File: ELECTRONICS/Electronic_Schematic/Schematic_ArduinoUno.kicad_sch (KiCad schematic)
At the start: 25 parts

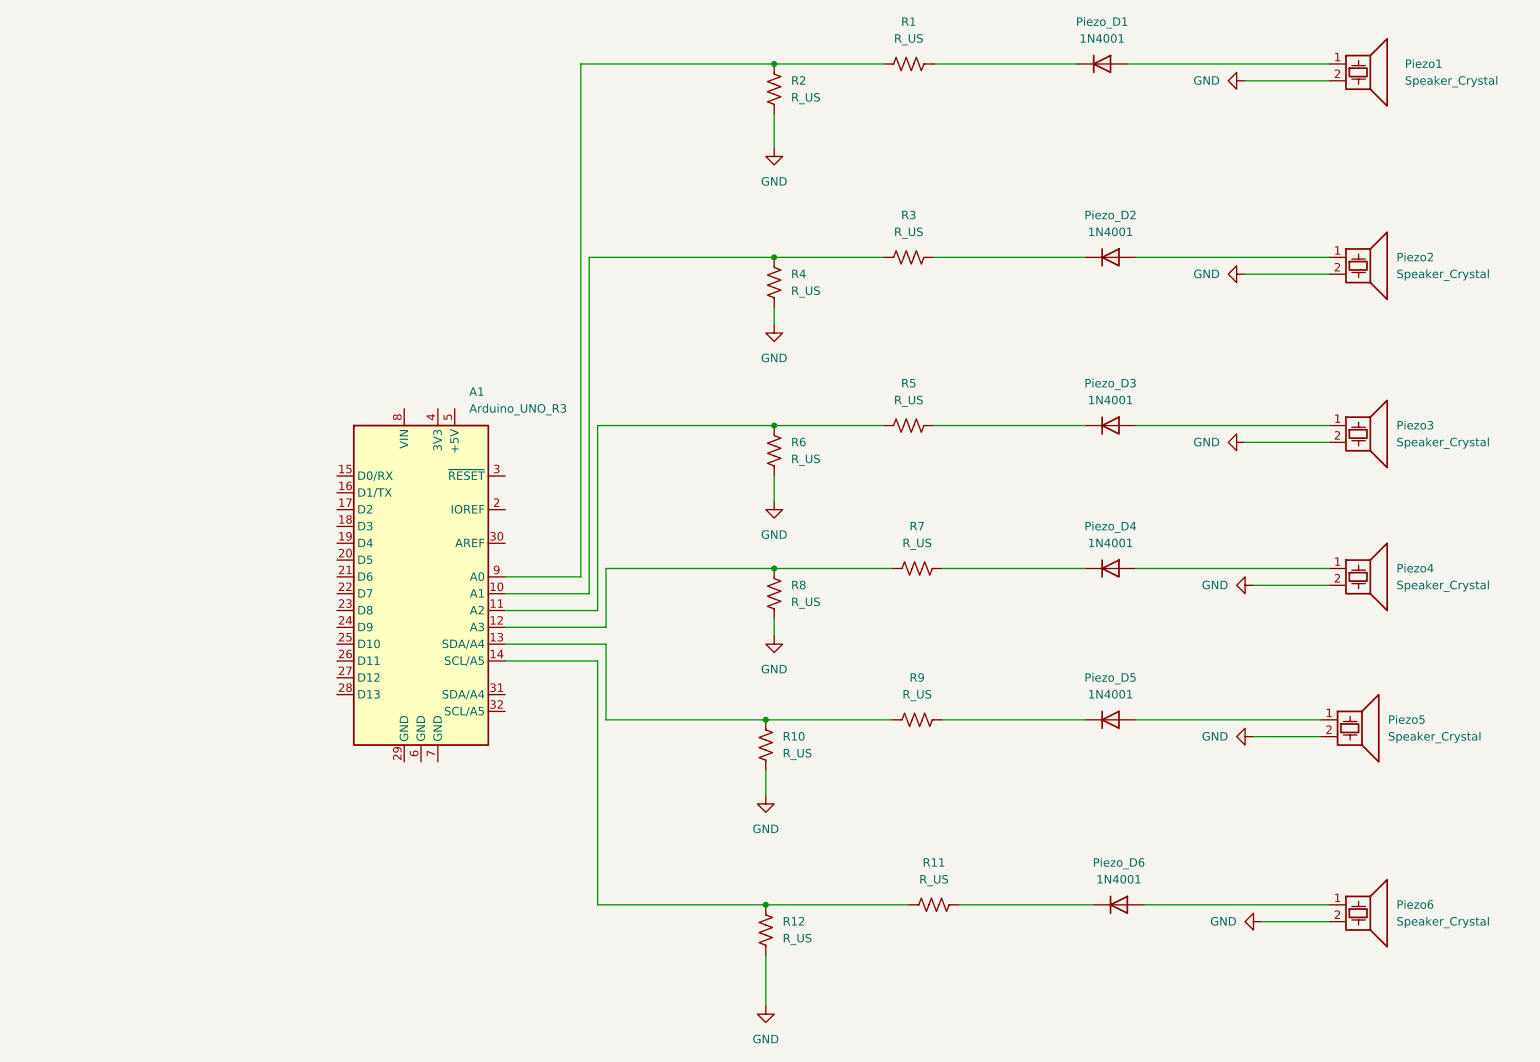
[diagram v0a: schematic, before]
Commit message: added revision 3 of schematic
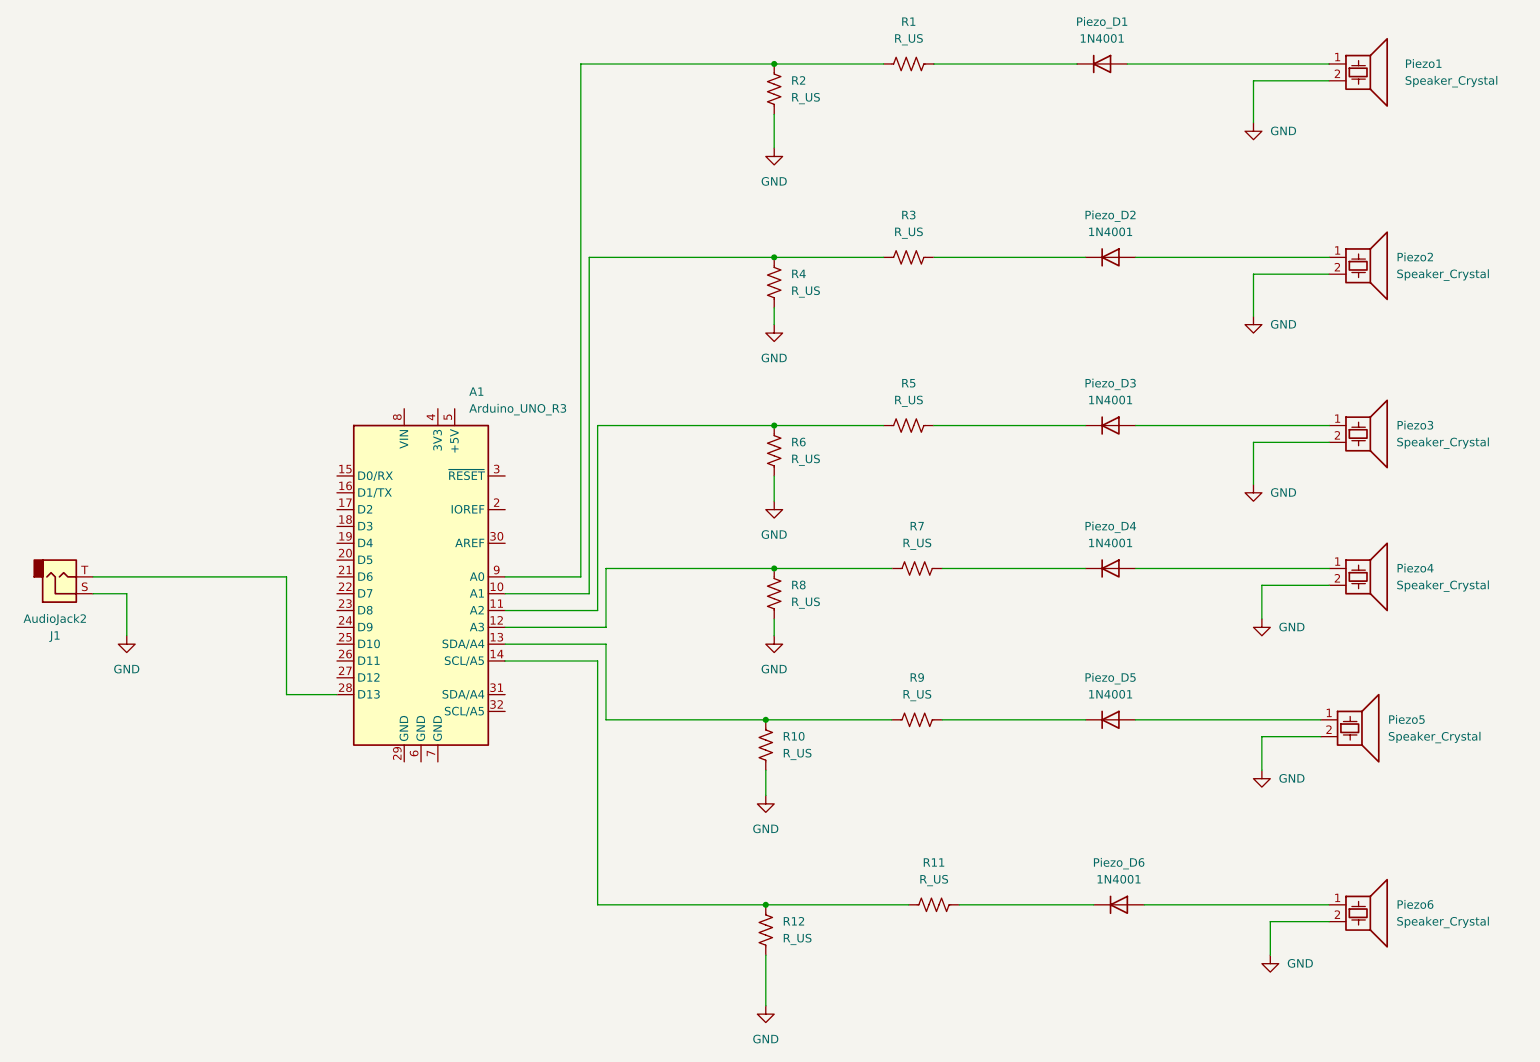
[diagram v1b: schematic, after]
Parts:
- added J1: AudioJack2, symbol Connector_Audio:AudioJack2
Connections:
- net GND: now also J1.S
- net at A1.28 (D13): now also J1.T
